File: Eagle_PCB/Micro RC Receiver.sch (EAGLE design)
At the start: 22 parts, among them IC2 TB6612FNG, Q1 CSTCC8M00G53-R0, U1 MIC5205-3.3, U2 ATMEGA328P_TQFP

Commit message: V 1.3
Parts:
- added C3: 10uF, SparkFun-Capacitors:10UF-16V-10%(TANT)
- added R2: 20k, rcl:R-EU_R0805
- added R3: 10k, rcl:R-EU_R0805
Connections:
- net A7: now also R2.1, R3.2
- net D3: now also IC2.PWMB; no longer IC2.BIN1
- net D5: now also IC2.BIN1; no longer IC2.PWMB
- net GND: now also C3.-, R3.1
- net VBAT: now also C3.+, R2.2
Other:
- note added: "2.4GHz Receiver with 4 servo outputs and dual DC motor driver V1.3"
- note added: "Battery voltage monitor"
- note added: "Designed July - Nov. 2016 by TheDIYGuy999"
- note removed: "2.4GHz Receiver with 4 servo outputs and dual DC motor driver"
- note removed: "Designed July 2016 by TheDIYGuy999"
- moved on the sheet: C5, C6
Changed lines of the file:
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@@
 <part name="JP10" library="00_custom_pinhead" deviceset="PINHD-1X2" device=""/>
 <part name="Q1" library="00_custom" deviceset="CSTCC" device="" technology="8M00G53-R0"/>
+<part name="R2" library="rcl" deviceset="R-EU_" device="R0805" value="20k"/>
+<part name="R3" library="rcl" deviceset="R-EU_" device="R0805" value="10k"/>
+<part name="GND17" library="supply1" deviceset="GND" device=""/>
+<part name="C3" library="SparkFun-Capacitors" deviceset="10UF-16V-10%(TANT)" device="" value="10uF"/>
+<part name="GND18" library="supply1" deviceset="GND" device=""/>
 </parts>
 <sheets>
@@
 <text x="291.592" y="8.382" size="2.54" layer="91">2.4GHz Receiver with 4
 servo outputs and dual
-DC motor driver</text>
-<text x="226.06" y="12.7" size="1.778" layer="91">Designed July 2016
+DC motor driver V1.3</text>
+<text x="213.36" y="12.7" size="1.778" layer="91">Designed July - Nov. 2016
 by TheDIYGuy999</text>
 <text x="340.36" y="68.58" size="1.778" layer="91">Serial Header</text>
@@
 <text x="177.8" y="198.12" size="1.778" layer="91">8MHz Resonator</text>
 <text x="35.56" y="129.54" size="1.778" layer="91">or LP2985AIM5-3.3</text>
+<text x="35.56" y="111.76" size="1.778" layer="91">Battery voltage monitor</text>
 </plain>
 <instances>
@@
 <instance part="JP2" gate="G$1" x="172.72" y="99.06" rot="R180"/>
 <instance part="GND7" gate="1" x="193.04" y="60.96"/>
-<instance part="GND11" gate="1" x="264.16" y="60.96"/>
+<instance part="GND11" gate="1" x="292.1" y="60.96"/>
 <instance part="IC2" gate="G$1" x="203.2" y="106.68"/>
-<instance part="P+4" gate="VCC" x="276.86" y="116.84"/>
-<instance part="C6" gate="G$1" x="276.86" y="71.12"/>
+<instance part="P+4" gate="VCC" x="304.8" y="116.84"/>
+<instance part="C6" gate="G$1" x="304.8" y="71.12"/>
 <instance part="C4" gate="G$1" x="233.68" y="71.12"/>
-<instance part="GND12" gate="1" x="276.86" y="60.96"/>
+<instance part="GND12" gate="1" x="304.8" y="60.96"/>
 <instance part="GND9" gate="1" x="233.68" y="60.96"/>
-<instance part="C5" gate="G$1" x="246.38" y="71.12"/>
-<instance part="GND10" gate="1" x="246.38" y="60.96"/>
+<instance part="C5" gate="G$1" x="261.62" y="71.12"/>
+<instance part="GND10" gate="1" x="261.62" y="60.96"/>
 <instance part="JP1" gate="G$1" x="22.86" y="231.14" rot="R180"/>
 <instance part="GND2" gate="1" x="55.88" y="213.36"/>
@@
 <instance part="JP10" gate="G$1" x="340.36" y="40.64" rot="R180"/>
 <instance part="Q1" gate="G$1" x="203.2" y="190.5" rot="R270"/>
+<instance part="R2" gate="G$1" x="45.72" y="88.9" rot="R90"/>
+<instance part="R3" gate="G$1" x="45.72" y="68.58" rot="R90"/>
+<instance part="GND17" gate="1" x="45.72" y="55.88"/>
+<instance part="C3" gate="G$1" x="246.38" y="71.12"/>
+<instance part="GND18" gate="1" x="246.38" y="60.96"/>
 </instances>
 <busses>
@@
 </segment>
 <segment>
-<wire x1="231.14" y1="88.9" x2="264.16" y2="88.9" width="0.1524" layer="91"/>
+<wire x1="231.14" y1="88.9" x2="292.1" y2="88.9" width="0.1524" layer="91"/>
 <pinref part="GND11" gate="1" pin="GND"/>
-<wire x1="264.16" y1="88.9" x2="264.16" y2="63.5" width="0.1524" layer="91"/>
+<wire x1="292.1" y1="88.9" x2="292.1" y2="63.5" width="0.1524" layer="91"/>
 <pinref part="IC2" gate="G$1" pin="GND"/>
 </segment>
@@
 <pinref part="C6" gate="G$1" pin="2"/>
 <pinref part="GND12" gate="1" pin="GND"/>
-<wire x1="276.86" y1="66.04" x2="276.86" y2="63.5" width="0.1524" layer="91"/>
+<wire x1="304.8" y1="66.04" x2="304.8" y2="63.5" width="0.1524" layer="91"/>
 </segment>
 <segment>
@@
 <pinref part="C5" gate="G$1" pin="2"/>
 <pinref part="GND10" gate="1" pin="GND"/>
-<wire x1="246.38" y1="66.04" x2="246.38" y2="63.5" width="0.1524" layer="91"/>
+<wire x1="261.62" y1="66.04" x2="261.62" y2="63.5" width="0.1524" layer="91"/>
 </segment>
 <segment>
@@
 <pinref part="GND16" gate="1" pin="GND"/>
 <wire x1="355.6" y1="124.46" x2="355.6" y2="121.92" width="0.1524" layer="91"/>
+</segment>
+<segment>
+<pinref part="GND17" gate="1" pin="GND"/>
+<pinref part="R3" gate="G$1" pin="1"/>
+<wire x1="45.72" y1="58.42" x2="45.72" y2="63.5" width="0.1524" layer="91"/>
+</segment>
+<segment>
+<pinref part="GND18" gate="1" pin="GND"/>
+<pinref part="C3" gate="G$1" pin="-"/>
+<wire x1="246.38" y1="63.5" x2="246.38" y2="66.04" width="0.1524" layer="91"/>
 </segment>
 </net>
@@
 </segment>
 <segment>
-<wire x1="231.14" y1="91.44" x2="276.86" y2="91.44" width="0.1524" layer="91"/>
-<wire x1="276.86" y1="91.44" x2="276.86" y2="93.98" width="0.1524" layer="91"/>
-<wire x1="276.86" y1="93.98" x2="276.86" y2="114.3" width="0.1524" layer="91"/>
-<wire x1="231.14" y1="93.98" x2="276.86" y2="93.98" width="0.1524" layer="91"/>
-<junction x="276.86" y="93.98"/>
+<wire x1="231.14" y1="91.44" x2="304.8" y2="91.44" width="0.1524" layer="91"/>
+<wire x1="304.8" y1="91.44" x2="304.8" y2="93.98" width="0.1524" layer="91"/>
+<wire x1="304.8" y1="93.98" x2="304.8" y2="114.3" width="0.1524" layer="91"/>
+<wire x1="231.14" y1="93.98" x2="304.8" y2="93.98" width="0.1524" layer="91"/>
+<junction x="304.8" y="93.98"/>
 <pinref part="IC2" gate="G$1" pin="STBY"/>
 <pinref part="IC2" gate="G$1" pin="VCC"/>
 <pinref part="P+4" gate="VCC" pin="VCC"/>
 <pinref part="C6" gate="G$1" pin="1"/>
-<wire x1="276.86" y1="91.44" x2="276.86" y2="73.66" width="0.1524" layer="91"/>
-<junction x="276.86" y="91.44"/>
+<wire x1="304.8" y1="91.44" x2="304.8" y2="73.66" width="0.1524" layer="91"/>
+<junction x="304.8" y="91.44"/>
 </segment>
 <segment>
@@
 </segment>
 <segment>
+<wire x1="231.14" y1="81.28" x2="236.22" y2="81.28" width="0.1524" layer="91"/>
+<label x="236.22" y="81.28" size="1.778" layer="95" xref="yes"/>
+<pinref part="IC2" gate="G$1" pin="PWMB"/>
+</segment>
+</net>
+<net name="D4" class="0">
+<segment>
+<pinref part="U2" gate="U$1" pin="PD4(XCK/T0)"/>
+<wire x1="271.78" y1="185.42" x2="276.86" y2="185.42" width="0.1524" layer="91"/>
+<label x="276.86" y="185.42" size="1.778" layer="95" xref="yes"/>
+</segment>
+<segment>
+<wire x1="231.14" y1="96.52" x2="236.22" y2="96.52" width="0.1524" layer="91"/>
+<label x="236.22" y="96.52" size="1.778" layer="95" xref="yes"/>
+<pinref part="IC2" gate="G$1" pin="AIN1"/>
+</segment>
+</net>
+<net name="D5" class="0">
+<segment>
+<pinref part="U2" gate="U$1" pin="PD5(T1)"/>
+<wire x1="271.78" y1="182.88" x2="287.02" y2="182.88" width="0.1524" layer="91"/>
+<label x="287.02" y="182.88" size="1.778" layer="95" xref="yes"/>
+</segment>
+<segment>
 <wire x1="231.14" y1="86.36" x2="236.22" y2="86.36" width="0.1524" layer="91"/>
 <label x="236.22" y="86.36" size="1.778" layer="95" xref="yes"/>
@@
 </segment>
 </net>
-<net name="D4" class="0">
-<segment>
-<pinref part="U2" gate="U$1" pin="PD4(XCK/T0)"/>
-<wire x1="271.78" y1="185.42" x2="276.86" y2="185.42" width="0.1524" layer="91"/>
-<label x="276.86" y="185.42" size="1.778" layer="95" xref="yes"/>
-</segment>
-<segment>
-<wire x1="231.14" y1="96.52" x2="236.22" y2="96.52" width="0.1524" layer="91"/>
-<label x="236.22" y="96.52" size="1.778" layer="95" xref="yes"/>
-<pinref part="IC2" gate="G$1" pin="AIN1"/>
-</segment>
-</net>
-<net name="D5" class="0">
-<segment>
-<pinref part="U2" gate="U$1" pin="PD5(T1)"/>
-<wire x1="271.78" y1="182.88" x2="287.02" y2="182.88" width="0.1524" layer="91"/>
-<label x="287.02" y="182.88" size="1.778" layer="95" xref="yes"/>
-</segment>
-<segment>
-<wire x1="231.14" y1="81.28" x2="236.22" y2="81.28" width="0.1524" layer="91"/>
-<label x="236.22" y="81.28" size="1.778" layer="95" xref="yes"/>
-<pinref part="IC2" gate="G$1" pin="PWMB"/>
-</segment>
-</net>
 <net name="D6" class="0">
 <segment>
@@
 <wire x1="271.78" y1="200.66" x2="276.86" y2="200.66" width="0.1524" layer="91"/>
 <label x="276.86" y="200.66" size="1.778" layer="95" xref="yes"/>
+</segment>
+<segment>
+<pinref part="R3" gate="G$1" pin="2"/>
+<pinref part="R2" gate="G$1" pin="1"/>
+<wire x1="45.72" y1="73.66" x2="45.72" y2="78.74" width="0.1524" layer="91"/>
+<wire x1="45.72" y1="78.74" x2="45.72" y2="83.82" width="0.1524" layer="91"/>
+<wire x1="45.72" y1="78.74" x2="55.88" y2="78.74" width="0.1524" layer="91"/>
+<junction x="45.72" y="78.74"/>
+<label x="55.88" y="78.74" size="1.778" layer="95" xref="yes"/>
 </segment>
 </net>
@@
 <wire x1="233.68" y1="76.2" x2="246.38" y2="76.2" width="0.1524" layer="91"/>
 <pinref part="C5" gate="G$1" pin="1"/>
-<wire x1="246.38" y1="76.2" x2="246.38" y2="73.66" width="0.1524" layer="91"/>
+<wire x1="246.38" y1="76.2" x2="261.62" y2="76.2" width="0.1524" layer="91"/>
+<wire x1="261.62" y1="76.2" x2="261.62" y2="73.66" width="0.1524" layer="91"/>
+<pinref part="C3" gate="G$1" pin="+"/>
+<wire x1="246.38" y1="73.66" x2="246.38" y2="76.2" width="0.1524" layer="91"/>
+<junction x="246.38" y="76.2"/>
 </segment>
 <segment>
@@
 <label x="363.22" y="127" size="1.778" layer="95" xref="yes"/>
 </segment>
-</net>
+<segment>
+<pinref part="R2" gate="G$1" pin="2"/>
+<wire x1="45.72" y1="93.98" x2="45.72" y2="99.06" width="0.1524" layer="91"/>
+<label x="45.72" y="99.06" size="1.778" layer="95" rot="R90" xref="yes"/>
+</segment>
+</net>

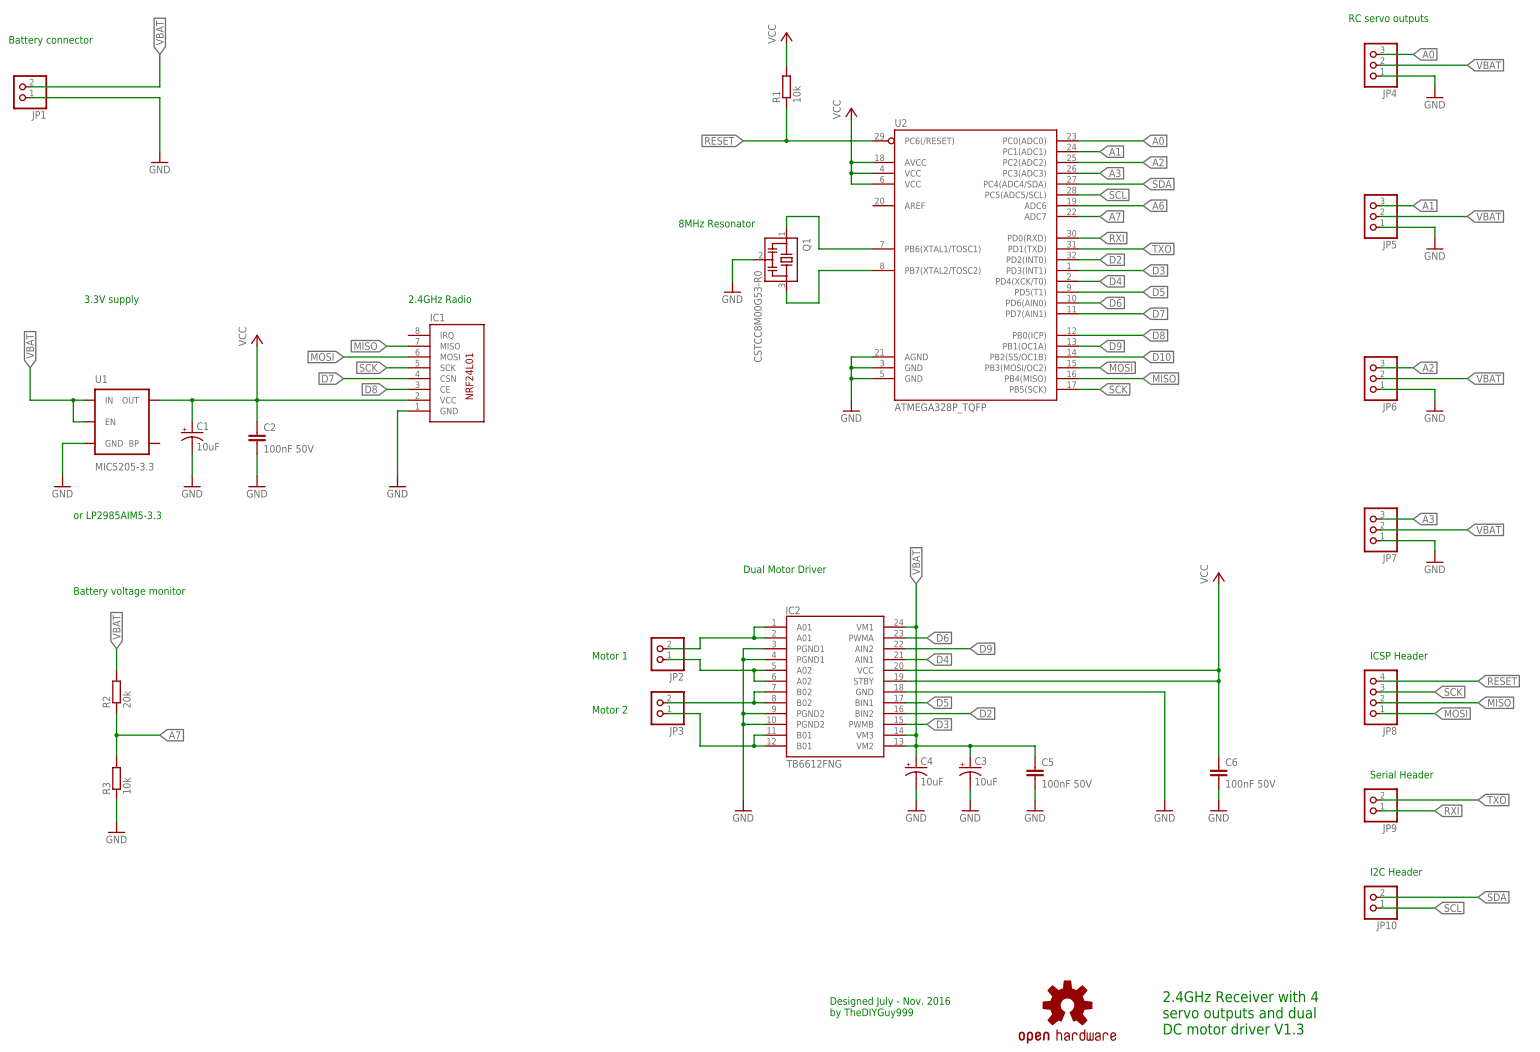
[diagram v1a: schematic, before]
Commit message: V1.4
GND plane and decoupling improved
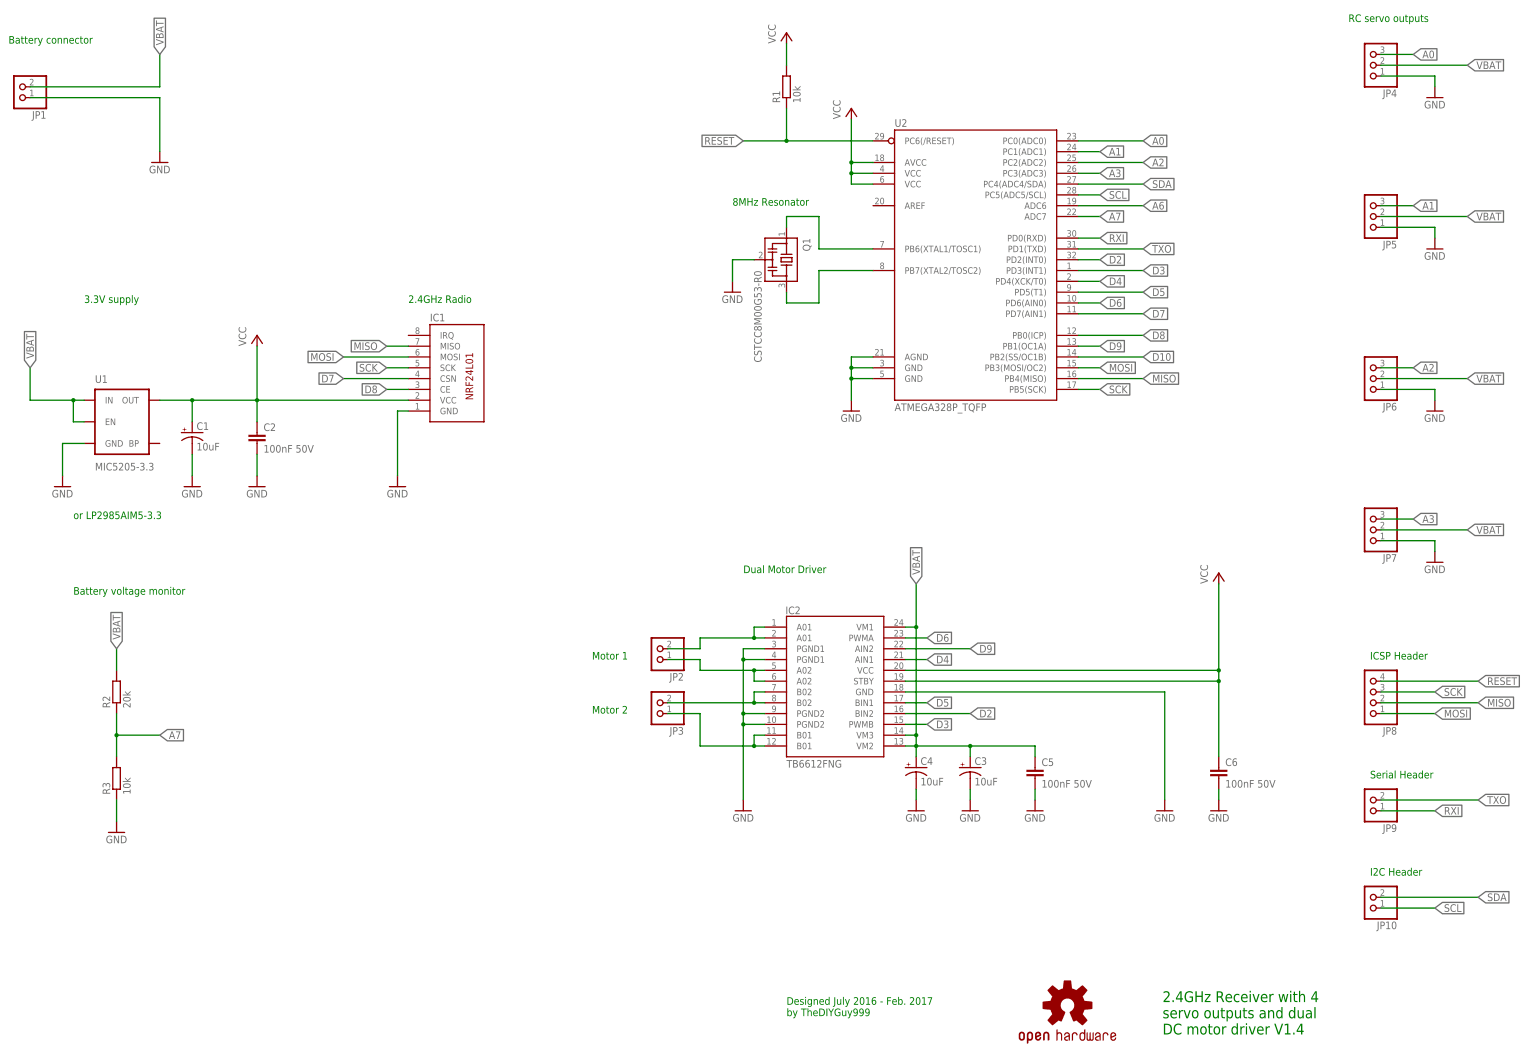
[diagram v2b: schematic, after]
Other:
- note added: "2.4GHz Receiver with 4 servo outputs and dual DC motor driver V1.4"
- note added: "Designed July 2016 - Feb. 2017 by TheDIYGuy999"
- note removed: "2.4GHz Receiver with 4 servo outputs and dual DC motor driver V1.3"
- note removed: "Designed July - Nov. 2016 by TheDIYGuy999"
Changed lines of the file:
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@@
 <text x="291.592" y="8.382" size="2.54" layer="91">2.4GHz Receiver with 4
 servo outputs and dual
-DC motor driver V1.3</text>
-<text x="213.36" y="12.7" size="1.778" layer="91">Designed July - Nov. 2016
+DC motor driver V1.4</text>
+<text x="203.2" y="12.7" size="1.778" layer="91">Designed July 2016 - Feb. 2017
 by TheDIYGuy999</text>
 <text x="340.36" y="68.58" size="1.778" layer="91">Serial Header</text>
 <text x="340.36" y="96.52" size="1.778" layer="91">ICSP Header</text>
 <text x="340.36" y="45.72" size="1.778" layer="91">I2C Header</text>
-<text x="177.8" y="198.12" size="1.778" layer="91">8MHz Resonator</text>
+<text x="190.5" y="203.2" size="1.778" layer="91">8MHz Resonator</text>
 <text x="35.56" y="129.54" size="1.778" layer="91">or LP2985AIM5-3.3</text>
 <text x="35.56" y="111.76" size="1.778" layer="91">Battery voltage monitor</text>

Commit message: V1.5: board slightly optimised, Gerbers included
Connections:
- net GND: now also IC1.GND@1
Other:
- note added: "2.4GHz Receiver with 4 servo outputs and dual DC motor driver V1.5"
- note added: "Dual Motor Driver (optional)"
- note removed: "2.4GHz Receiver with 4 servo outputs and dual DC motor driver V1.4"
- note removed: "Dual Motor Driver"
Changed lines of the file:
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@@
 <part name="C3" library="SparkFun-Capacitors" deviceset="10UF-16V-10%(TANT)" device="" value="10uF"/>
 <part name="GND18" library="supply1" deviceset="GND" device=""/>
+<part name="GND19" library="supply1" deviceset="GND" device=""/>
 </parts>
 <sheets>
@@
 <text x="157.48" y="83.82" size="1.778" layer="91">Motor 2</text>
 <text x="157.48" y="96.52" size="1.778" layer="91">Motor 1</text>
-<text x="193.04" y="116.84" size="1.778" layer="91">Dual Motor Driver</text>
+<text x="193.04" y="116.84" size="1.778" layer="91">Dual Motor Driver
+(optional)</text>
 <text x="20.32" y="241.3" size="1.778" layer="91">Battery connector</text>
 <text x="38.1" y="180.34" size="1.778" layer="91">3.3V supply</text>
@@
 <text x="291.592" y="8.382" size="2.54" layer="91">2.4GHz Receiver with 4
 servo outputs and dual
-DC motor driver V1.4</text>
+DC motor driver V1.5</text>
 <text x="203.2" y="12.7" size="1.778" layer="91">Designed July 2016 - Feb. 2017
 by TheDIYGuy999</text>
@@
 <instance part="C3" gate="G$1" x="246.38" y="71.12"/>
 <instance part="GND18" gate="1" x="246.38" y="60.96"/>
+<instance part="GND19" gate="1" x="144.78" y="137.16"/>
 </instances>
 <busses>
@@
 <wire x1="246.38" y1="63.5" x2="246.38" y2="66.04" width="0.1524" layer="91"/>
 </segment>
+<segment>
+<pinref part="IC1" gate="G$1" pin="GND@1"/>
+<pinref part="GND19" gate="1" pin="GND"/>
+<wire x1="142.24" y1="154.94" x2="144.78" y2="154.94" width="0.1524" layer="91"/>
+<wire x1="144.78" y1="154.94" x2="144.78" y2="139.7" width="0.1524" layer="91"/>
+</segment>
 </net>
